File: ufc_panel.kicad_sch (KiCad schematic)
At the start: 101 parts, among them J1 Conn_01x20_Socket, Q1 BC817-25LT1G, SW1 SW_Push_45deg, SW10 SW_Push_45deg, SW11 SW_Push_45deg, SW12 SW_Push_45deg, SW13 SW_Push_45deg, SW14 SW_Push_45deg, SW15 SW_Push_45deg, SW16 SW_Push_45deg, SW17 SW_Push_45deg, SW18 SW_Push_45deg, SW19 SW_Push_45deg, SW2 SW_Push_45deg, SW20 SW_Push_45deg, SW21 SW_Push_45deg, SW22 SW_Push_45deg, SW23 SW_Push_45deg, SW24 SW_Push_45deg, SW25 SW_Push_45deg, SW26 SW_Push_45deg, SW27 SW_Push_45deg, SW28 SW_Push_45deg, SW29 SW_Push_45deg, SW3 SW_Push_45deg, SW30 SW_Push_45deg, SW31 SW_Push_45deg, SW32 SW_Push_45deg, SW33 SW_Push_45deg, SW34 SW_Push_45deg, SW35 SW_Push_45deg, SW4 SW_Push_45deg, SW5 SW_Push_45deg, SW6 SW_Push_45deg, SW7 SW_Push_45deg, SW8 SW_Push_45deg, SW9 SW_Push_45deg

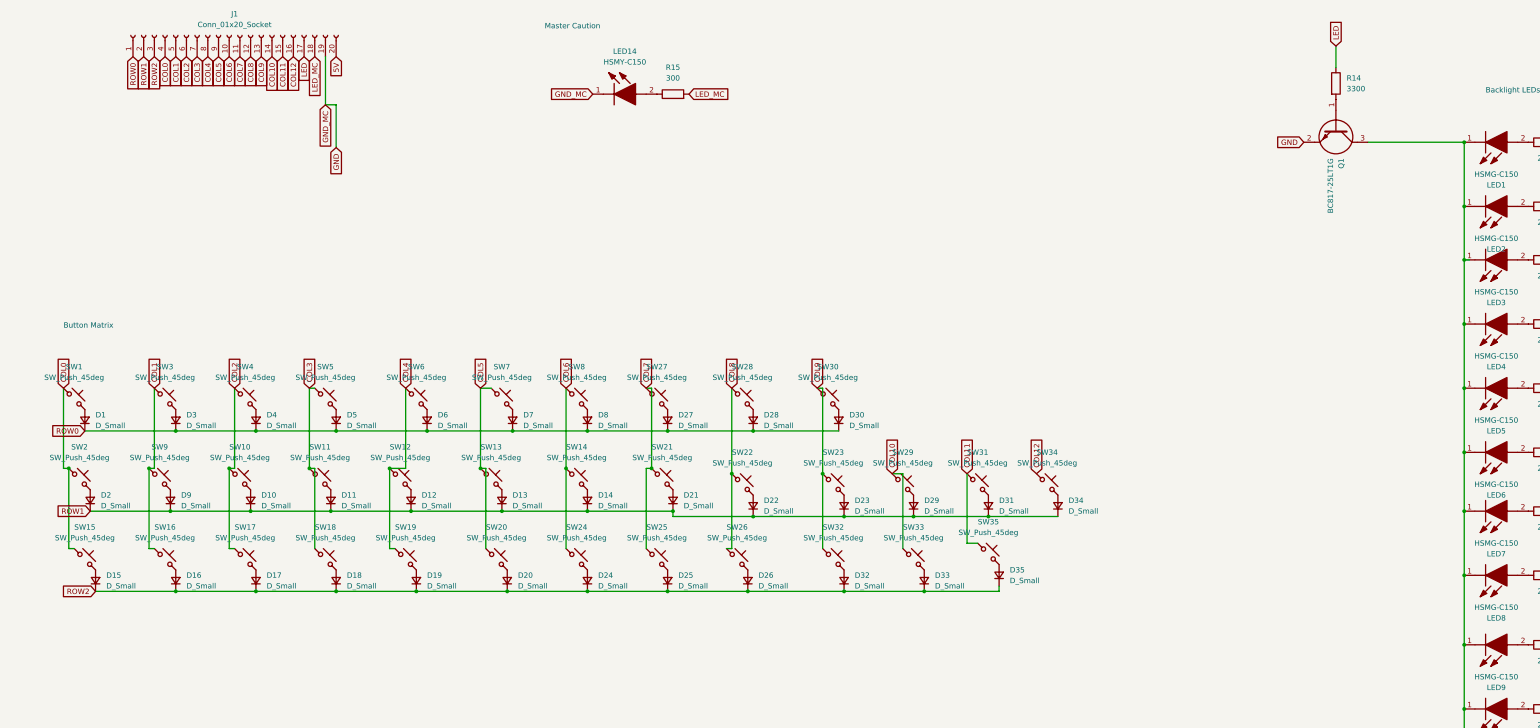
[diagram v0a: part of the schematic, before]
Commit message: feat: new version - v1.1; redesigned traces, connector, etc
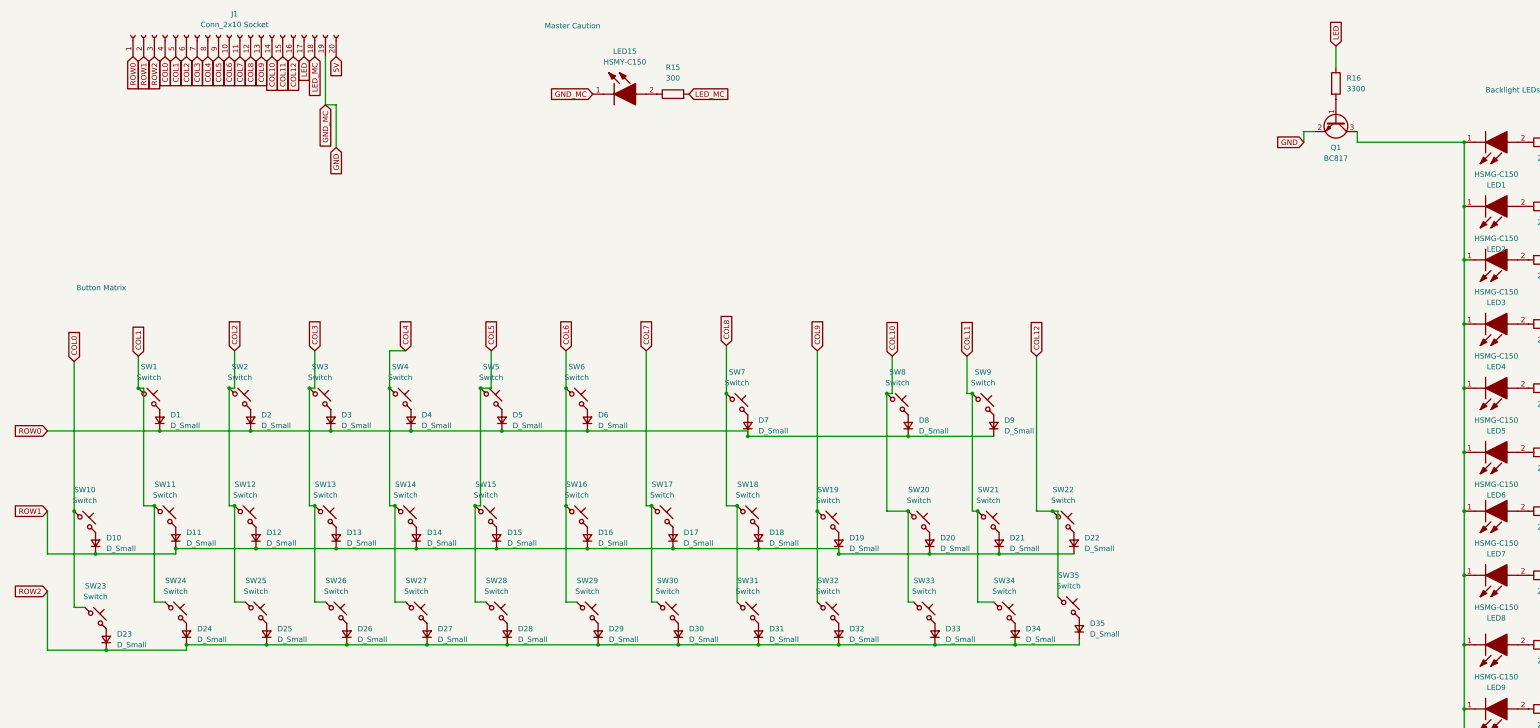
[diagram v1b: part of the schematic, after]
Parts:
- removed Q1: BC817-25LT1G, MOUSER:SOT96P237X111-3N, symbol MOUSER:BC817-25LT1G
- added Q1: BC817, Package_TO_SOT_SMD:SOT-23, symbol Transistor_BJT:BC817
- J1: value Conn_01x20_Socket -> Conn_2x10 Socket; footprint Connector_PinHeader_1.00mm:PinHeader_2x10_P1.00mm_Vertical -> Connector_PinHeader_2.54mm:PinHeader_1x20_P2.54mm_Vertical
- LED1, LED10, LED11, LED12, LED13, LED2, LED3, LED4, LED5, LED6, LED7, LED8, LED9: footprint MOUSER:LEDC3216X120N -> LED_SMD:LED_1206_3216Metric_Pad1.42x1.75mm_HandSolder
- LED15: renamed from LED14; footprint MOUSER:LEDC3216X120N -> LED_SMD:LED_1206_3216Metric_Pad1.42x1.75mm_HandSolder
- SW1, SW35: value SW_Push_45deg -> Switch
- SW10: renamed from SW30; value SW_Push_45deg -> Switch
- SW11: renamed from SW2; value SW_Push_45deg -> Switch
- SW12: renamed from SW9; value SW_Push_45deg -> Switch
- SW13: renamed from SW10; value SW_Push_45deg -> Switch
- SW14: renamed from SW11; value SW_Push_45deg -> Switch
- SW15: renamed from SW12; value SW_Push_45deg -> Switch
- SW16: renamed from SW13; value SW_Push_45deg -> Switch
- SW17: renamed from SW14; value SW_Push_45deg -> Switch
- SW18: renamed from SW21; value SW_Push_45deg -> Switch
- SW19: renamed from SW22; value SW_Push_45deg -> Switch
- SW2: renamed from SW3; value SW_Push_45deg -> Switch
- SW20: renamed from SW23; value SW_Push_45deg -> Switch
- SW21: renamed from SW29; value SW_Push_45deg -> Switch
- SW22: renamed from SW31; value SW_Push_45deg -> Switch
- SW23: renamed from SW34; value SW_Push_45deg -> Switch
- SW24: renamed from SW15; value SW_Push_45deg -> Switch
- SW25: renamed from SW16; value SW_Push_45deg -> Switch
- SW26: renamed from SW17; value SW_Push_45deg -> Switch
- SW27: renamed from SW18; value SW_Push_45deg -> Switch
- SW28: renamed from SW19; value SW_Push_45deg -> Switch
- SW29: renamed from SW20; value SW_Push_45deg -> Switch
- SW3: renamed from SW4; value SW_Push_45deg -> Switch
- SW30: renamed from SW24; value SW_Push_45deg -> Switch
- SW31: renamed from SW25; value SW_Push_45deg -> Switch
- SW32: renamed from SW26; value SW_Push_45deg -> Switch
- SW33: renamed from SW32; value SW_Push_45deg -> Switch
- SW34: renamed from SW33; value SW_Push_45deg -> Switch
- SW4: renamed from SW5; value SW_Push_45deg -> Switch
- SW5: renamed from SW6; value SW_Push_45deg -> Switch
- SW6: renamed from SW7; value SW_Push_45deg -> Switch
- SW7: renamed from SW8; value SW_Push_45deg -> Switch
- SW8: renamed from SW27; value SW_Push_45deg -> Switch
- SW9: renamed from SW28; value SW_Push_45deg -> Switch
- renumbered D30 to D10, D2 to D11, D9 to D12, D10 to D13, D11 to D14, D12 to D15, D13 to D16, D14 to D17, D21 to D18, D22 to D19, D3 to D2, D23 to D20, D29 to D21, D31 to D22, D34 to D23, D15 to D24, D16 to D25, D17 to D26, D18 to D27, D19 to D28, D20 to D29, D4 to D3, D24 to D30, D25 to D31, D26 to D32, D32 to D33, D33 to D34, D5 to D4, D6 to D5, D7 to D6, D8 to D7, D27 to D8, D28 to D9, R14 to R16
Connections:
- net COL0: now also SW10.1, SW23.1; no longer SW1.1, SW11.1, SW24.1
- net COL1: now also SW1.1, SW11.1, SW24.1; no longer SW12.1, SW2.1, SW25.1
- net COL10: now also SW20.1, SW33.1, SW8.1; no longer SW21.1, SW34.1
- net COL11: now also SW21.1, SW34.1, SW9.1; no longer SW22.1, SW35.1
- net COL12: now also SW22.1, SW35.1; no longer SW23.1
- net COL2: now also SW12.1, SW2.1, SW25.1; no longer SW13.1, SW26.1, SW3.1
- net COL3: now also SW13.1, SW26.1, SW3.1; no longer SW14.1, SW27.1, SW4.1
- net COL4: now also SW14.1, SW27.1, SW4.1; no longer SW15.1, SW28.1, SW5.1
- net COL5: now also SW15.1, SW28.1, SW5.1; no longer SW16.1, SW29.1, SW6.1
- net COL6: now also SW16.1, SW29.1, SW6.1; no longer SW17.1, SW30.1, SW7.1
- net COL7: now also SW17.1, SW30.1; no longer SW18.1, SW31.1, SW8.1
- net COL8: now also SW18.1, SW31.1, SW7.1; no longer SW19.1, SW32.1, SW9.1
- net COL9: now also SW19.1, SW32.1; no longer SW10.1, SW20.1, SW33.1
- net GND: now also Q1.2 (E)
- net ROW0: no longer D10.1 (K)
- net ROW1: now also D10.1 (K); no longer D23.1 (K)
- net ROW2: now also D23.1 (K)
- net at LED1.1 (K), LED10.1 (K), LED11.1 (K)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: now also Q1.3 (C)
- net at R16.2: now also Q1.1 (B)
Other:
- moved on the sheet: D1, D10, D11, D12, D13, D14, D15, D16, D17, D18, D19, D2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
